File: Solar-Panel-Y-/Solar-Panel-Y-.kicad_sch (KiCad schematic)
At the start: 59 parts, among them J1 FFC2B28-10-G, J2 BATTERY CONNECTOR, J3 B2B-PH-SM4-TB_LF__SN_, U1 Value, U2 TSL2561, U3 SW_SPDT, U4 SW_SPDT

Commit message: Exported Gerbers
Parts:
- added H1, H2, H3, H4: MountingHole, MountingHole:MountingHole_2.2mm_M2_DIN965, symbol Mechanical:MountingHole
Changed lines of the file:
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@@
     (pin "2")
+  )
+  (symbol (lib_id "Mechanical:MountingHole") (at 185.039 92.075 0) (unit 1)
+    (in_bom yes) (on_board yes) (fields_autoplaced)
+    (property "Reference" "H1" (id 0) (at 187.579 91.2403 0)
+      (effects (font (size 1.27 1.27)) (justify left))
+    )
+    (property "Value" "MountingHole" (id 1) (at 187.579 93.7772 0)
+      (effects (font (size 1.27 1.27)) (justify left))
+    )
+    (property "Footprint" "MountingHole:MountingHole_2.2mm_M2_DIN965" (id 2) (at 185.039 92.075 0)
+      (effects (font (size 1.27 1.27)) hide)
+    )
+    (property "Datasheet" "~" (id 3) (at 185.039 92.075 0)
+      (effects (font (size 1.27 1.27)) hide)
+    )
   )
   (symbol (lib_id "Device:C_Small") (at 200.914 73.152 0) (unit 1)
@@
     (pin "1")
     (pin "2")
+  )
+  (symbol (lib_id "Mechanical:MountingHole") (at 185.039 104.521 0) (unit 1)
+    (in_bom yes) (on_board yes) (fields_autoplaced)
+    (property "Reference" "H3" (id 0) (at 187.579 103.6863 0)
+      (effects (font (size 1.27 1.27)) (justify left))
+    )
+    (property "Value" "MountingHole" (id 1) (at 187.579 106.2232 0)
+      (effects (font (size 1.27 1.27)) (justify left))
+    )
+    (property "Footprint" "MountingHole:MountingHole_2.2mm_M2_DIN965" (id 2) (at 185.039 104.521 0)
+      (effects (font (size 1.27 1.27)) hide)
+    )
+    (property "Datasheet" "~" (id 3) (at 185.039 104.521 0)
+      (effects (font (size 1.27 1.27)) hide)
+    )
   )
   (symbol (lib_id "Connector_Generic:Conn_02x05_Odd_Even") (at 306.705 147.193 0) (unit 1)
@@
     (pin "2")
   )
+  (symbol (lib_id "Mechanical:MountingHole") (at 185.039 98.298 0) (unit 1)
+    (in_bom yes) (on_board yes) (fields_autoplaced)
+    (property "Reference" "H2" (id 0) (at 187.579 97.4633 0)
+      (effects (font (size 1.27 1.27)) (justify left))
+    )
+    (property "Value" "MountingHole" (id 1) (at 187.579 100.0002 0)
+      (effects (font (size 1.27 1.27)) (justify left))
+    )
+    (property "Footprint" "MountingHole:MountingHole_2.2mm_M2_DIN965" (id 2) (at 185.039 98.298 0)
+      (effects (font (size 1.27 1.27)) hide)
+    )
+    (property "Datasheet" "~" (id 3) (at 185.039 98.298 0)
+      (effects (font (size 1.27 1.27)) hide)
+    )
+  )
+  (symbol (lib_id "Mechanical:MountingHole") (at 185.166 110.871 0) (unit 1)
+    (in_bom yes) (on_board yes) (fields_autoplaced)
+    (property "Reference" "H4" (id 0) (at 187.706 110.0363 0)
+      (effects (font (size 1.27 1.27)) (justify left))
+    )
+    (property "Value" "MountingHole" (id 1) (at 187.706 112.5732 0)
+      (effects (font (size 1.27 1.27)) (justify left))
+    )
+    (property "Footprint" "MountingHole:MountingHole_2.2mm_M2_DIN965" (id 2) (at 185.166 110.871 0)
+      (effects (font (size 1.27 1.27)) hide)
+    )
+    (property "Datasheet" "~" (id 3) (at 185.166 110.871 0)
+      (effects (font (size 1.27 1.27)) hide)
+    )
+  )
   (sheet_instances
     (path "/" (page "1"))
@@
       (reference "D5") (unit 1) (value "SBDiode") (footprint "solarpanels:SB Diode")
     )
+    (path "/2bd8e8f1-1a24-4dbc-9d3e-02ec45243012"
+      (reference "H1") (unit 1) (value "MountingHole") (footprint "MountingHole:MountingHole_2.2mm_M2_DIN965")
+    )
+    (path "/f33292b6-e256-451d-9bfa-7d07ba9e670f"
+      (reference "H2") (unit 1) (value "MountingHole") (footprint "MountingHole:MountingHole_2.2mm_M2_DIN965")
+    )
+    (path "/3b5c237f-d7d6-49ed-b03e-6a11bbbe8b45"
+      (reference "H3") (unit 1) (value "MountingHole") (footprint "MountingHole:MountingHole_2.2mm_M2_DIN965")
+    )
+    (path "/f61337de-df22-47d1-92dc-eb1819702425"
+      (reference "H4") (unit 1) (value "MountingHole") (footprint "MountingHole:MountingHole_2.2mm_M2_DIN965")
+    )
     (path "/47dd0e95-7a8d-4f29-bb90-29c26f742b3a"

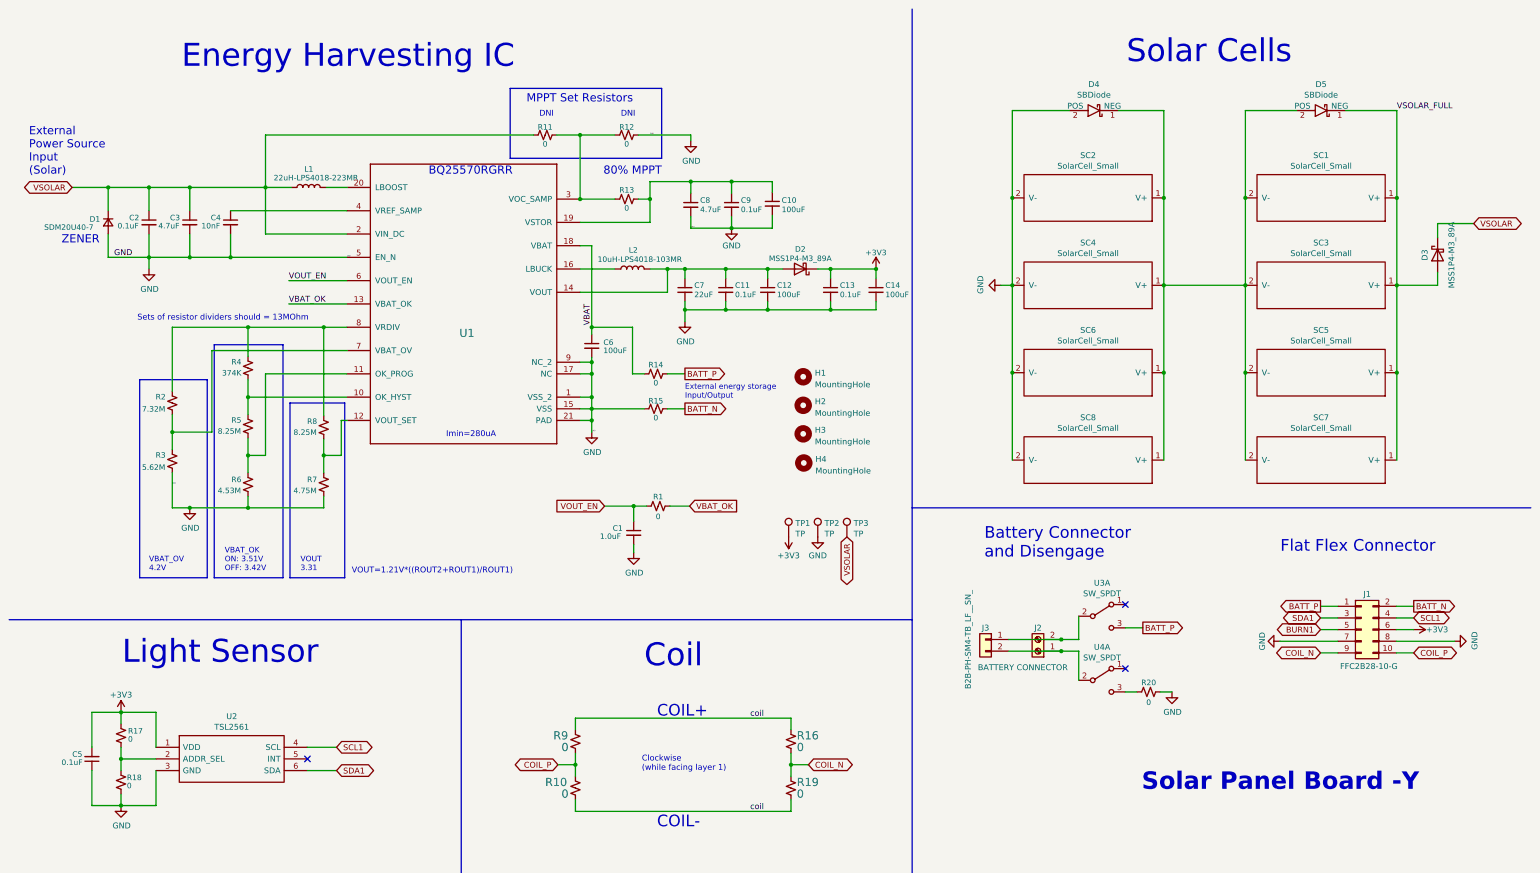
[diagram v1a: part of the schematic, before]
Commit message: Stack architecture schematic updates / fixes
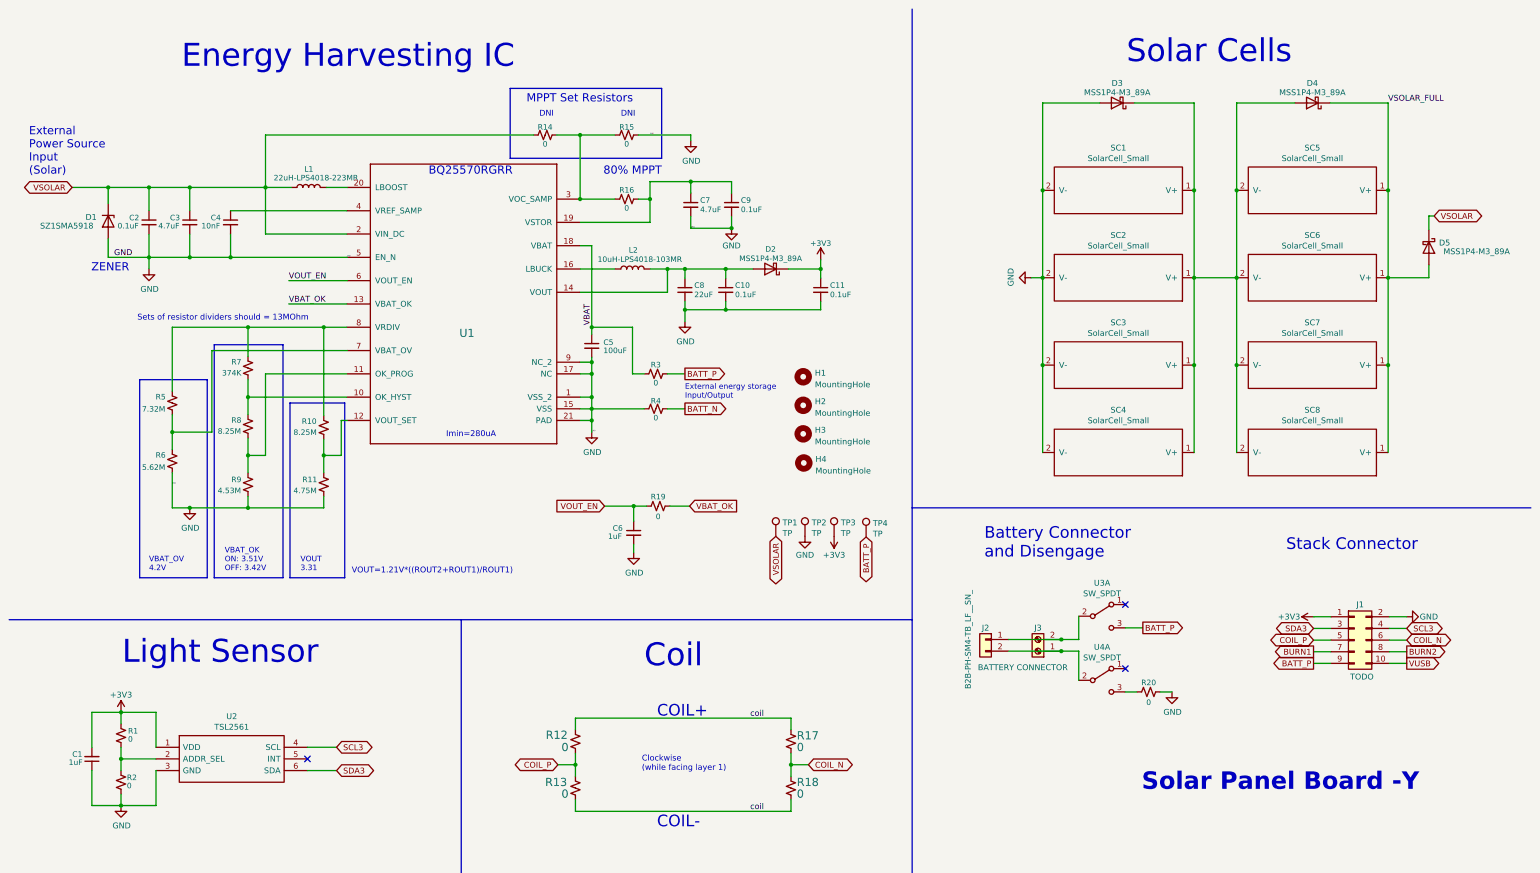
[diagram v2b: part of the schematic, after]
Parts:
- removed C10: 100uF, Capacitor_SMD:C_0603_1608Metric, symbol Device:C_Small
- removed C12, C14: 100uF, Capacitor_SMD:C_0402_1005Metric, symbol Device:C_Small
- removed D1: SDM20U40-7, Diode_SMD:D_SOD-523, symbol Device:D_Small
- removed D4, D5: SBDiode, solarpanels:SB Diode, symbol solarpanels:SBDiode
- added D1: SZ1SMA5918, Diode_SMD:D_SMA, symbol Diode:Z1SMAxxx
- added D3, D4: MSS1P4-M3_89A, solarpanels:MICROSMP, symbol Device:D_Schottky
- added TP4: TP, TestPoint:TestPoint_THTPad_D1.0mm_Drill0.5mm, symbol Connector:TestPoint
- C1: renamed from C5; value 0.1uF -> 1uF; footprint Capacitor_SMD:C_0402_1005Metric -> Capacitor_SMD:C_0603_1608Metric
- C10: renamed from C11; footprint Capacitor_SMD:C_0402_1005Metric -> Capacitor_SMD:C_0603_1608Metric
- C11: renamed from C13; footprint Capacitor_SMD:C_0402_1005Metric -> Capacitor_SMD:C_0603_1608Metric
- C2, C3, C4, C9: footprint Capacitor_SMD:C_0402_1005Metric -> Capacitor_SMD:C_0603_1608Metric
- C5: renamed from C6; footprint Capacitor_SMD:C_0603_1608Metric -> Capacitor_SMD:C_0805_2012Metric
- C6: renamed from C1; value 1.0uF -> 1uF; footprint Capacitor_SMD:C_0402_1005Metric -> Capacitor_SMD:C_0603_1608Metric
- C7: renamed from C8; footprint Capacitor_SMD:C_0402_1005Metric -> Capacitor_SMD:C_0603_1608Metric
- C8: renamed from C7; footprint Capacitor_SMD:C_0402_1005Metric -> Capacitor_SMD:C_0603_1608Metric
- J1: value FFC2B28-10-G -> TODO
- R1: renamed from R17; footprint Resistor_SMD:R_0402_1005Metric -> Resistor_SMD:R_0603_1608Metric
- R10: renamed from R8; footprint Resistor_SMD:R_0402_1005Metric -> Resistor_SMD:R_0603_1608Metric
- R11: renamed from R7; footprint Resistor_SMD:R_0402_1005Metric -> Resistor_SMD:R_0603_1608Metric
- R12: renamed from R9; footprint Resistor_SMD:R_0402_1005Metric -> Resistor_SMD:R_0603_1608Metric
- R13: renamed from R10; footprint Resistor_SMD:R_0402_1005Metric -> Resistor_SMD:R_0603_1608Metric
- R14: renamed from R11; footprint Resistor_SMD:R_0402_1005Metric -> Resistor_SMD:R_0603_1608Metric
- R15: renamed from R12; footprint Resistor_SMD:R_0402_1005Metric -> Resistor_SMD:R_0603_1608Metric
- R16: renamed from R13; footprint Resistor_SMD:R_0402_1005Metric -> Resistor_SMD:R_0603_1608Metric
- R17: renamed from R16; footprint Resistor_SMD:R_0402_1005Metric -> Resistor_SMD:R_0603_1608Metric
- R18: renamed from R19; footprint Resistor_SMD:R_0402_1005Metric -> Resistor_SMD:R_0603_1608Metric
- R19: renamed from R1; footprint Resistor_SMD:R_0402_1005Metric -> Resistor_SMD:R_0603_1608Metric
- R2: renamed from R18; footprint Resistor_SMD:R_0402_1005Metric -> Resistor_SMD:R_0603_1608Metric
- R20: footprint Resistor_SMD:R_0402_1005Metric -> Resistor_SMD:R_0603_1608Metric
- R3: renamed from R14; footprint Resistor_SMD:R_0402_1005Metric -> Resistor_SMD:R_0603_1608Metric
- R4: renamed from R15; footprint Resistor_SMD:R_0402_1005Metric -> Resistor_SMD:R_0603_1608Metric
- R5: renamed from R2; footprint Resistor_SMD:R_0402_1005Metric -> Resistor_SMD:R_0603_1608Metric
- R6: renamed from R3; footprint Resistor_SMD:R_0402_1005Metric -> Resistor_SMD:R_0603_1608Metric
- R7: renamed from R4; footprint Resistor_SMD:R_0402_1005Metric -> Resistor_SMD:R_0603_1608Metric
- R8: renamed from R5; footprint Resistor_SMD:R_0402_1005Metric -> Resistor_SMD:R_0603_1608Metric
- R9: renamed from R6; footprint Resistor_SMD:R_0402_1005Metric -> Resistor_SMD:R_0603_1608Metric
- U1: value Value -> BQ25570RGRR
- renumbered D3 to D5, J3 to J2, J2 to J3, SC2 to SC1, SC4 to SC2, SC6 to SC3, SC8 to SC4, SC1 to SC5, SC3 to SC6, SC5 to SC7, SC7 to SC8
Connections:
- net +3V3: now also J1.1 (Pin_1), TP3.1; no longer J1.6 (Pin_6), TP1.1
- net BATT_N: no longer J1.2 (Pin_2)
- net BATT_P: now also J1.9 (Pin_9), TP4.1; no longer J1.1 (Pin_1)
- net BURN1: now also J1.7 (Pin_7); no longer J1.5 (Pin_5)
- net COIL_N: now also J1.6 (Pin_6); no longer J1.9 (Pin_9)
- net COIL_P: now also J1.5 (Pin_5); no longer J1.10 (Pin_10)
- net GND: now also J1.2 (Pin_2), D1.2 (A), D3.2 (A); no longer J1.7 (Pin_7), J1.8 (Pin_8)
- net VSOLAR: now also TP1.1, D1.1 (K); no longer TP3.1
- net VSOLAR_FULL: now also D4.1 (K)
- net at SC1.1 (V+), SC2.1 (V+), SC3.1 (V+)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: now also D3.1 (K), D4.2 (A)
- net SCL1 renamed SCL3
- net SDA1 renamed SDA3
- new net BURN2: J1.8 (Pin_8)
- new net VUSB: J1.10 (Pin_10)
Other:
- note added: "Stack Connector"
- note removed: "Flat Flex Connector"
- moved on the sheet: C11, D2, D5, SC1, SC2, SC3, SC4, SC5, SC6, SC7, SC8, TP1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

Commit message: X board updates
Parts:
- removed J2: B2B-PH-SM4-TB_LF__SN_, Connector_JST:JST_PH_B2B-PH-SM4-TB_1x02-1MP_P2.00mm_Vertical, symbol Connector_Generic:Conn_01x02
- removed J3: BATTERY CONNECTOR, solarpanels:SCREWTERMINAL-3.5MM-2_LOCK, symbol Connector:Screw_Terminal_01x02
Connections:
- net BURN1 is gone; now on net COIL_P: J1.7 (Pin_7)
- net BURN2 is gone; now on net SDA3: J1.8 (Pin_8)
- net +3V3: now also J1.4 (Pin_4); no longer J1.1 (Pin_1)
- net BATT_P: now also J1.3 (Pin_3); no longer J1.9 (Pin_9)
- net COIL_N: now also J1.9 (Pin_9); no longer J1.6 (Pin_6)
- net COIL_P: no longer J1.5 (Pin_5)
- net GND: now also J1.5 (Pin_5); no longer J1.2 (Pin_2)
- net SCL3: now also J1.6 (Pin_6); no longer J1.4 (Pin_4)
- net SDA3: no longer J1.3 (Pin_3)
- net BATT_P_SW: now reaches U3.2 (B)
- net BATT_P_SW: now also J1.2 (Pin_2)
- net BATT_N_SW: now reaches U4.2 (B)
- net BATT_N_SW: now also J1.1 (Pin_1)

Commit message: X Board Changes for new Y rails
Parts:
- removed R4: 0, Resistor_SMD:R_0603_1608Metric, symbol Device:R_Small_US
- added C12, C13: 10nF, Capacitor_SMD:C_0402_1005Metric, symbol Device:C
- added Q1, Q3: BSS138DWQ-7, Package_TO_SOT_SMD:SOT-363_SC-70-6, symbol mainboard:BSS138DWQ-7
- added Q2, Q4: MBT2222ADW1T1, Package_TO_SOT_SMD:SOT-363_SC-70-6, symbol Transistor_BJT:MBT2222ADW1T1
- added R21, R28: 100K, Resistor_SMD:R_0402_1005Metric, symbol Device:R_US
- added R22, R23: 0, Resistor_SMD:R_0402_1005Metric, symbol Device:R_US
- added R24, R25, R29, R30: 10K, Resistor_SMD:R_0402_1005Metric, symbol Device:R_US
- added R26, R31: 200K, Resistor_SMD:R_0402_1005Metric, symbol Device:R_US
- added R27, R4: 680, Resistor_SMD:R_0402_1005Metric, symbol Device:R_US
- C1, C10, C11, C2, C3, C4, C6, C7, C8, C9: footprint Capacitor_SMD:C_0603_1608Metric -> Capacitor_SMD:C_0402_1005Metric
- D1: value SZ1SMA5918 -> SZMM5Z5V1T1G; footprint Diode_SMD:D_SMA -> Diode_SMD:D_SOD-523
- H1, H2, H3, H4: footprint MountingHole:MountingHole_2.2mm_M2_DIN965 -> MountingHole:MountingHole_2.2mm_M2_DIN965_Pad; symbol Mechanical:MountingHole -> Mechanical:MountingHole_Pad
- J1: value TODO -> FTS-105-01-L-DV-A; footprint solarpanels:GCT_FFC2B28-10-G -> batteryboard:FTS-105-XX-YY-DV-A
- R1, R10, R11, R12, R13, R14, R15, R16, R17, R18, R19, R2, R20, R3, R5, R6, R7, R8, R9: footprint Resistor_SMD:R_0603_1608Metric -> Resistor_SMD:R_0402_1005Metric
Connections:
- net +3V3: now also R21.1, R24.1, R25.1, R28.1, R29.1, R30.1
- net GND: now also H1.1, H2.1, H3.1, H4.1, C12.2, C13.2, Q1.1 (S2), Q1.4 (S1), Q3.1 (S2), Q3.4 (S1)
- net SCL3: now also Q2.1 (E1), Q2.3 (C2), R22.2
- net SDA3: now also Q4.1 (E1), Q4.3 (C2), R23.2
- new net: Q1.6 (D1), Q2.5 (B2), R24.2, R4.2
- new net: Q3.6 (D1), Q4.5 (B2), R27.2, R29.2
- new net: Q4.2 (B1), R27.1
- new net: Q3.2 (G2), Q3.3 (D2), R28.2
- new net: Q1.2 (G2), Q1.3 (D2), R21.2
- new net: C12.1, Q1.5 (G1), R26.2
- new net: Q2.2 (B1), R4.1
- new net: C13.1, Q3.5 (G1), R31.2
- new net SCL_LS: Q2.4 (E2), Q2.6 (C1), R22.1, R25.2, R26.1
- new net SDA_LS: Q4.4 (E2), Q4.6 (C1), R23.1, R30.2, R31.1
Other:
- note added: "I2C Bus Protection - Light Sensor"
- note added: "To Mainboard"

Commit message: Finished Y- Board
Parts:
- SW1: renamed from U3; footprint solarpanels:D2F-L2-2 -> solarpanels:D2F-L2-A1; symbol Switch:SW_DPDT_x2 -> Switch:SW_SPDT
- SW2: renamed from U4; footprint solarpanels:D2F-L2 -> solarpanels:D2F-L2-A; symbol Switch:SW_DPDT_x2 -> Switch:SW_SPDT
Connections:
- net BATT_P: no longer TP4.1
- net SCL3: no longer U2.4 (SCL)
- net SCL_LS: now also U2.4 (SCL)
- net SDA3: no longer U2.6 (SDA)
- net SDA_LS: now also U2.6 (SDA)
- net VBAT: now also TP4.1
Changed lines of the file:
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@@
+    )
+  )
+  (global_label "SDA_LS" (shape bidirectional) (at 83.312 177.927 0) (fields_autoplaced)
+    (effects (font (size 1.27 1.27)) (justify left))
+    (property "Intersheet References" "${INTERSHEET_REFS}" (id 0) (at 92.4095 177.8476 0)
+      (effects (font (size 1.27 1.27)) (justify left) hide)
     )
   )
@@
     )
   )
-  (global_label "SDA3" (shape bidirectional) (at 83.312 177.927 0) (fields_autoplaced)
-    (effects (font (size 1.27 1.27)) (justify left))
-    (property "Intersheet References" "${INTERSHEET_REFS}" (id 0) (at 90.4138 177.8476 0)
-      (effects (font (size 1.27 1.27)) (justify left) hide)
-    )
-  )
   (global_label "SDA_LS" (shape bidirectional) (at 383.54 109.474 0) (fields_autoplaced)
     (effects (font (size 1.27 1.27)) (justify left))
@@
     )
   )
-  (global_label "SCL3" (shape bidirectional) (at 83.312 172.847 0) (fields_autoplaced)
-    (effects (font (size 1.27 1.27)) (justify left))
-    (property "Intersheet References" "${INTERSHEET_REFS}" (id 0) (at 90.3533 172.7676 0)
-      (effects (font (size 1.27 1.27)) (justify left) hide)
-    )
-  )
   (global_label "VSOLAR" (shape bidirectional) (at 322.58 57.023 0) (fields_autoplaced)
     (effects (font (size 1.27 1.27)) (justify left))
@@
     )
   )
+  (global_label "SCL_LS" (shape input) (at 83.312 172.847 0) (fields_autoplaced)
+    (effects (font (size 1.27 1.27)) (justify left))
+    (property "Intersheet References" "${INTERSHEET_REFS}" (id 0) (at 92.3491 172.7676 0)
+      (effects (font (size 1.27 1.27)) (justify left) hide)
+    )
+  )
   (global_label "VBAT_OK" (shape input) (at 160.274 120.269 0) (fields_autoplaced)
     (effects (font (size 1.27 1.27)) (justify left))
@@
     )
   )
-  (global_label "BATT_P" (shape bidirectional) (at 198.755 127 270) (fields_autoplaced)
+  (global_label "VBAT" (shape bidirectional) (at 198.755 127 270) (fields_autoplaced)
     (effects (font (size 1.27 1.27)) (justify right))
-    (property "Intersheet References" "${INTERSHEET_REFS}" (id 0) (at 198.6756 135.8556 90)
+    (property "Intersheet References" "${INTERSHEET_REFS}" (id 0) (at 198.6756 133.739 90)
       (effects (font (size 1.27 1.27)) (justify right) hide)
     )
@@
     (pin "2")
   )
-  (symbol (lib_id "Switch:SW_DPDT_x2") (at 250.19 144.272 0) (unit 1)
-    (in_bom yes) (on_board yes)
-    (property "Reference" "U3" (id 0) (at 250.19 137.033 0))
+  (symbol (lib_id "Switch:SW_SPDT") (at 250.19 144.272 0) (unit 1)
+    (in_bom yes) (on_board yes)
+    (property "Reference" "SW1" (id 0) (at 250.19 137.033 0))
     (property "Value" "SW_SPDT" (id 1) (at 250.19 139.3444 0))
-    (property "Footprint" "solarpanels:D2F-L2-2" (id 2) (at 250.19 144.272 0)
+    (property "Footprint" "solarpanels:D2F-L2-A1" (id 2) (at 250.19 144.272 0)
       (effects (font (size 1.27 1.27)) hide)
     )
@@
     (pin "2")
     (pin "3")
-    (pin "4")
-    (pin "5")
-    (pin "6")
-  )
-  (symbol (lib_id "Switch:SW_DPDT_x2") (at 250.19 158.242 0) (unit 1)
-    (in_bom yes) (on_board yes)
-    (property "Reference" "U4" (id 0) (at 250.19 151.003 0))
+  )
+  (symbol (lib_id "Switch:SW_SPDT") (at 250.19 158.242 0) (unit 1)
+    (in_bom yes) (on_board yes)
+    (property "Reference" "SW2" (id 0) (at 250.19 151.003 0))
     (property "Value" "SW_SPDT" (id 1) (at 250.19 153.3144 0))
-    (property "Footprint" "solarpanels:D2F-L2" (id 2) (at 250.19 158.242 0)
+    (property "Footprint" "solarpanels:D2F-L2-A" (id 2) (at 250.19 158.242 0)
       (effects (font (size 1.27 1.27)) hide)
     )
@@
     (pin "2")
     (pin "3")
-    (pin "4")
-    (pin "5")
-    (pin "6")
   )
   (symbol (lib_id "Device:R_Small_US") (at 260.35 160.782 90) (unit 1)
@@
       (reference "SC8") (unit 1) (value "SolarCell_Small") (footprint "solarpanels:KXOB25-05X3F")
     )
+    (path "/00000000-0000-0000-0000-00005dc81e30"
+      (reference "SW1") (unit 1) (value "SW_SPDT") (footprint "solarpanels:D2F-L2-A1")
+    )
+    (path "/00000000-0000-0000-0000-00005dcb22ff"
+      (reference "SW2") (unit 1) (value "SW_SPDT") (footprint "solarpanels:D2F-L2-A")
+    )
     (path "/00000000-0000-0000-0000-00005df6b470"
       (reference "TP1") (unit 1) (value "TP") (footprint "TestPoint:TestPoint_THTPad_D1.0mm_Drill0.5mm")
@@
       (reference "U2") (unit 1) (value "TSL2561") (footprint "solarpanels:TSL2561")
     )
-    (path "/00000000-0000-0000-0000-00005dc81e30"
-      (reference "U3") (unit 1) (value "SW_SPDT") (footprint "solarpanels:D2F-L2-2")
-    )
-    (path "/00000000-0000-0000-0000-00005dcb22ff"
-      (reference "U4") (unit 1) (value "SW_SPDT") (footprint "solarpanels:D2F-L2")
-    )
-  )
+  )

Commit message: Made Suggested Y- changes
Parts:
- removed SC3, SC7: SolarCell_Small, solarpanels:KXOB25-05X3F, symbol solarpanels:SolarCell_Small
- added J2: BM02B-SRSS-TB, Connector_JST:JST_SH_BM02B-SRSS-TB_1x02-1MP_P1.00mm_Vertical, symbol Connector_Generic:Conn_01x02
- H1, H2, H3, H4: footprint MountingHole:MountingHole_2.2mm_M2_DIN965_Pad -> MountingHole:MountingHole_3.2mm_M3_DIN965_Pad
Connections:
- net BATT_N_SW: now also J2.2 (Pin_2)
- net BATT_P_SW: now also J2.1 (Pin_1)
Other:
- moved on the sheet: R20, SW1, SW2
